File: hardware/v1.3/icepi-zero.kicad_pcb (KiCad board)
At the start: 4 copper layers, 65 x 30 mm, 159 parts, among them IC1 IS42S16160J-6BLI, J1 Conn_02x20_Counter_Clockwise, J2 GPDI_C_1.3, J3 USB_C_Receptacle_USB2.0_14P, J4 USB_C_Receptacle_USB2.0_14P, J5 USB_C_Receptacle_USB2.0_14P, J6 Micro_SD_Card_Det2, SW1 SW_Push, SW2 SW_Push, U1 ECP5-CABGA256, U10 TPD2EUSB30A, U12 W25Q128JVS, U2 TLV62569DBV, U3 TLV62569DBV, U4 TLV62569DBV, U5 TPD2EUSB30A, U6 PCA9306DC1, U7 TPD2EUSB30A, U8 TPD2EUSB30A, U9 FT231XQ, Y1 SG-8018CG 50.000000MHz

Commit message: 3.3V LDO
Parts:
- C34, L3: moved to B.Cu
- R11, R9: moved to F.Cu
- moved C34 53.2 mm to (160.7, 142.8)
- moved L3 49.3 mm to (160.7, 139.4), turned to -90 degrees
- moved R10 48.4 mm to (158.3, 140.3), turned to 90 degrees
- moved C35 47.4 mm to (159.3, 140.3), turned to 90 degrees
- moved U4 41.2 mm to (151.6, 136.6), turned to 90 degrees
- moved C33 39.9 mm to (149.0, 137.1), turned to 90 degrees
- moved R11 38.6 mm to (148.9, 135.1), turned to 180 degrees
- moved R9 6.53 mm to (151.2, 151.0), turned to 180 degrees
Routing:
- net Net-(U4-FB): track 0.00 -> 14.1 mm, vias 0 -> 1
- net +5V: track 59.4 -> 68.0 mm
- net +3V3: track 7.76 -> 12.9 mm
- net Net-(U3-FB): track 4.12 -> 6.06 mm
- net /SDRAM/D0: track 9.82 -> 8.54 mm

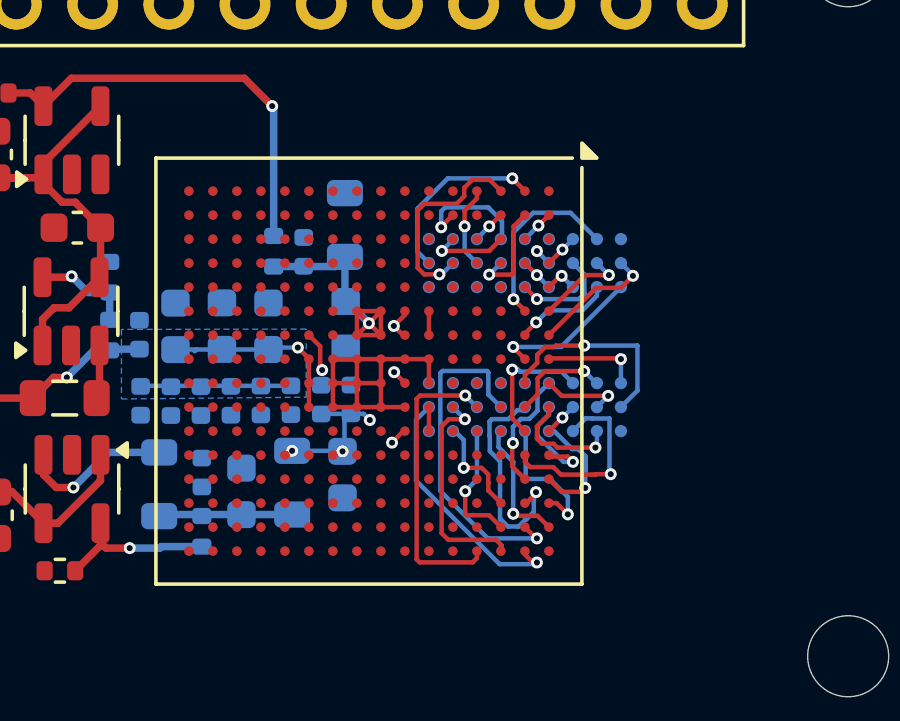
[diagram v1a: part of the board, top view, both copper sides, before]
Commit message: 3.3V memory fix
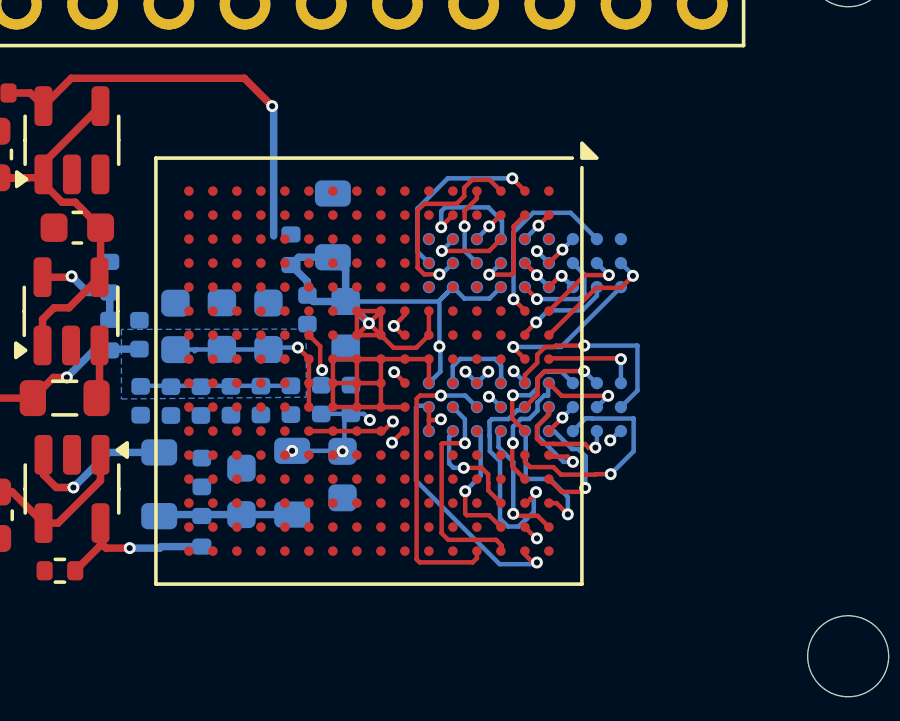
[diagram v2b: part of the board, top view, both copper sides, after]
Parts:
- moved C35 1.93 mm to (159.4, 142.3), turned to -90 degrees
- moved R10 0.58 mm to (158.8, 140.3)
- moved L3 0.40 mm to (160.2, 139.5)
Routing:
- net +3V3: track 12.9 -> 45.9 mm, vias 1 -> 8
- net /SDRAM/D6: track 11.3 -> 6.48 mm, vias 1 -> 2
- net GND: track 14.9 -> 17.9 mm
- net /SDRAM/~{CS}: track 6.53 -> 7.64 mm

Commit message: HDMI preparation
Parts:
- moved Y1 41.5 mm to (156.1, 136.4), turned to 180 degrees
- moved C1 40.5 mm to (156.9, 135.5), turned to 180 degrees
- moved C37 40.0 mm to (139.6, 150.9), turned to 90 degrees
- moved C38 38.9 mm to (140.0, 149.0), turned to 180 degrees
- moved C36 38.9 mm to (138.7, 150.9), turned to 90 degrees
- moved C39 38.2 mm to (140.0, 148.1), turned to 180 degrees
- moved C40 37.6 mm to (140.0, 147.2), turned to 180 degrees
- moved C41 37.0 mm to (140.0, 146.2), turned to 180 degrees
- moved C42 36.4 mm to (140.0, 145.3), turned to 180 degrees
- moved C43 35.9 mm to (140.0, 144.4), turned to 180 degrees
- moved R12 35.3 mm to (140.0, 143.5), turned to 0 degrees
- moved R13 34.8 mm to (140.0, 142.2), turned to 0 degrees
- moved R14 34.3 mm to (140.0, 141.3), turned to 0 degrees
- moved J2 32.5 mm to (136.7, 145.8), turned to -90 degrees
- moved C18 6.21 mm to (144.1, 152.9)
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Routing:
- net /SDRAM/A3: track 3.22 -> 14.6 mm
- net +5V: track 68.0 -> 77.1 mm
- net /GLOBAL_CLK: track 0.00 -> 3.78 mm
- net /GPDI/CONN_D2+: track 0.00 -> 3.53 mm
- net /GPDI/CONN_D2-: track 0.00 -> 3.02 mm
- net /SDRAM/D14: track 2.68 -> 5.45 mm
- net /GPDI/CONN_D1+: track 0.00 -> 2.35 mm
- net +3V3: track 45.9 -> 43.6 mm, vias 8 -> 9
- net Net-(J2-HPD): track 0.00 -> 2.07 mm
- net Net-(J2-UTILITY): track 0.00 -> 2.01 mm
- net Net-(J2-CEC): track 0.00 -> 2.00 mm
- net /GPDI/CONN_D1-: track 0.00 -> 1.99 mm
- net /GPDI/CONN_CK-: track 0.00 -> 1.98 mm
- net /GPDI/CONN_D0+: track 0.00 -> 1.94 mm
- net /GPDI/CONN_CK+: track 0.00 -> 1.77 mm
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
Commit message: HDMI preparation
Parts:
- R9: moved to B.Cu
- moved C36 14.6 mm to (124.5, 147.8)
- moved C38 14.6 mm to (125.8, 145.8)
- moved C40 14.6 mm to (125.8, 144.0)
- moved C41 14.6 mm to (125.8, 143.1)
- moved C42 14.6 mm to (125.8, 142.2)
- moved C43 14.6 mm to (125.8, 141.2)
- moved R12 14.6 mm to (125.8, 140.3)
- moved R13 14.6 mm to (125.8, 139.1)
- moved R14 14.6 mm to (125.8, 138.2)
- moved C39 14.6 mm to (125.8, 144.9)
- moved J2 14.6 mm to (122.5, 142.7)
- moved C37 14.6 mm to (125.4, 147.8)
- moved C18 1.27 mm to (143.2, 152.0), turned to 180 degrees
- moved R9 0.92 mm to (146.9, 153.0)
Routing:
- net /GPDI/GPDI_D0+: track 0.00 -> 38.8 mm
- net /GPDI/GPDI_CLK+: track 0.00 -> 37.3 mm
- net /GPDI/GPDI_D2+: track 0.00 -> 37.1 mm
- net /GPDI/GPDI_D1+: track 0.00 -> 36.8 mm
- net /GPDI/GPDI_D0-: track 0.00 -> 36.1 mm
- net /GPDI/GPDI_D1-: track 0.00 -> 36.0 mm
- net /GPDI/GPDI_CLK-: track 0.00 -> 35.6 mm
- net /GPDI/GPDI_D2-: track 0.00 -> 35.1 mm
- net +5V: track 77.1 -> 92.8 mm
- net Net-(U3-FB): track 6.06 -> 4.99 mm

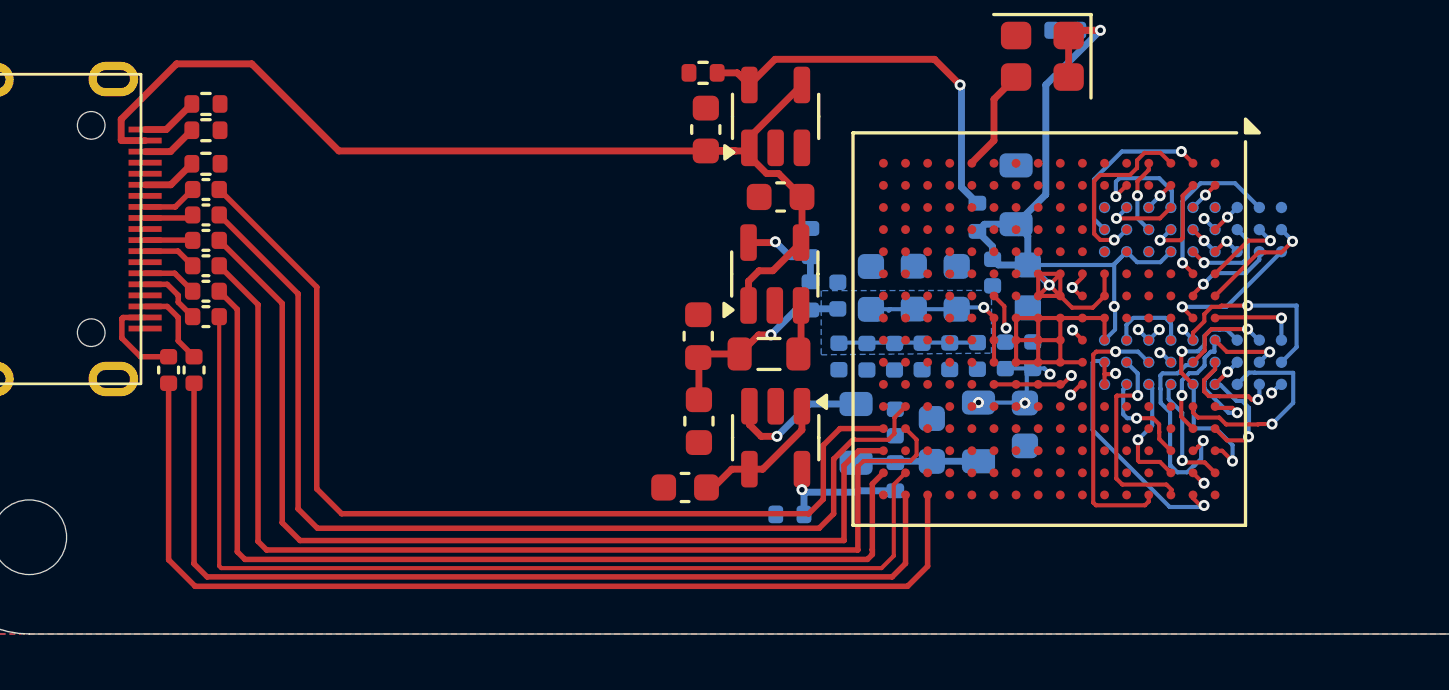
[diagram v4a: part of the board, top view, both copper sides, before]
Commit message: HDMI preparation, memory traces fix
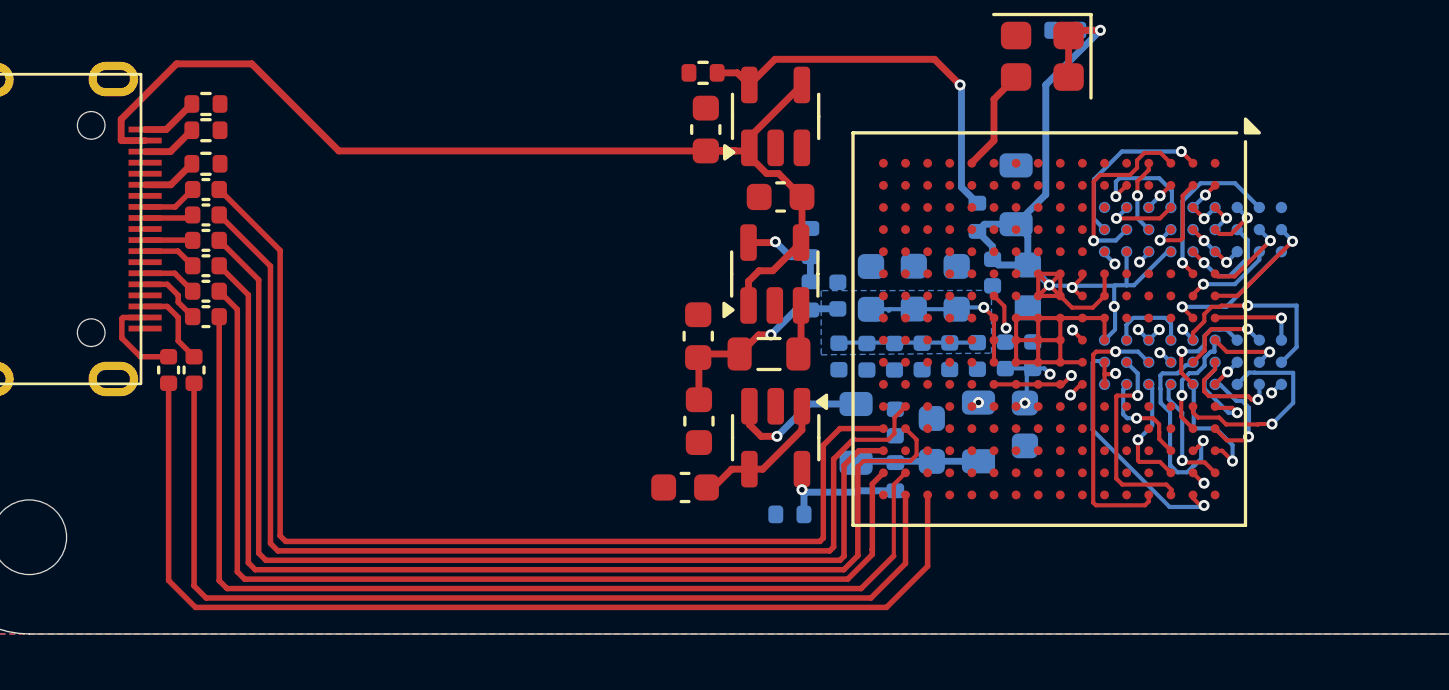
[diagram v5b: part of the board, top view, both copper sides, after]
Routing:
- net /SDRAM/A3: track 14.6 -> 3.22 mm
- net +3V3: track 43.6 -> 50.9 mm
- net /GPDI/GPDI_CLK-: track 35.6 -> 39.0 mm
- net /SDRAM/D14: track 5.45 -> 2.68 mm
- net /GPDI/GPDI_CLK+: track 37.3 -> 40.0 mm
- net /GPDI/GPDI_D0-: track 36.1 -> 38.2 mm
- net GND: track 17.9 -> 19.9 mm, vias 0 -> 2
- net /Power/FILTERED_2V5: track 13.5 -> 11.8 mm
- net /GPDI/GPDI_D0+: track 38.8 -> 40.2 mm
- net /SDRAM/DQM1: track 0.00 -> 1.14 mm, vias 0 -> 1
- net /GPDI/GPDI_D2-: track 35.1 -> 36.2 mm
- net /GPDI/GPDI_D2+: track 37.1 -> 38.2 mm
- net /GPDI/GPDI_D1-: track 36.0 -> 37.0 mm
- net /GPDI/GPDI_D1+: track 36.8 -> 37.7 mm
- net /SDRAM/A12: track 1.13 -> 2.01 mm
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
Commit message: GND fix
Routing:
- net GND: track 19.9 -> 24.8 mm
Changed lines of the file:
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@@
 	)
 	(segment
+		(start 159.925 151.495)
+		(end 160.151274 151.495)
+		(width 0.15)
+		(layer "F.Cu")
+		(net 16)
+	)
+	(segment
 		(start 157.525 147.495)
 		(end 155.125 147.495)
@@
 	)
 	(segment
+		(start 161.08 151.91)
+		(end 161.13 151.96)
+		(width 0.15)
+		(layer "F.Cu")
+		(net 16)
+	)
+	(segment
+		(start 160.301 140.719)
+		(end 161.901 140.719)
+		(width 0.15)
+		(layer "F.Cu")
+		(net 16)
+	)
+	(segment
+		(start 159.925 141.095)
+		(end 160.301 140.719)
+		(width 0.15)
+		(layer "F.Cu")
+		(net 16)
+	)
+	(segment
+		(start 161.901 140.719)
+		(end 162.325 140.295)
+		(width 0.15)
+		(layer "F.Cu")
+		(net 16)
+	)
+	(segment
 		(start 156.725 145.895)
 		(end 156.725 146.695)
@@
 	)
 	(segment
+		(start 160.151274 151.495)
+		(end 160.566274 151.91)
+		(width 0.15)
+		(layer "F.Cu")
+		(net 16)
+	)
+	(segment
+		(start 160.566274 151.91)
+		(end 161.08 151.91)
+		(width 0.15)
+		(layer "F.Cu")
+		(net 16)
+	)
+	(segment
 		(start 155.925 146.695)
 		(end 155.925 147.495)
@@
 	)
 	(segment
+		(start 161.13 151.96)
+		(end 161.13 152.73)
+		(width 0.15)
+		(layer "F.Cu")
+		(net 16)
+	)
+	(segment
 		(start 155.925 146.695)
 		(end 155.925 145.895)
@@
 	)
 	(segment
-		(start 160.761 141.293545)
-		(end 160.761 141.859)
+		(start 160.761 141.859)
+		(end 160.725 141.895)
 		(width 0.15)
 		(layer "B.Cu")
@@
 	)
 	(segment
-		(start 160.305 140.837545)
-		(end 160.761 141.293545)
+		(start 158.735 141.12291)
+		(end 158.81391 141.044)
 		(width 0.15)
 		(layer "B.Cu")
@@
 	)
 	(segment
-		(start 158.735 141.5)
-		(end 158.735 140.96509)
+		(start 160.761 141.293545)
+		(end 160.761 141.859)
 		(width 0.15)
 		(layer "B.Cu")
@@
 	)
 	(segment
-		(start 158.735 140.96509)
-		(end 158.862545 140.837545)
+		(start 158.81391 141.044)
+		(end 160.511455 141.044)
 		(width 0.15)
 		(layer "B.Cu")
@@
 	)
 	(segment
-		(start 160.761 141.859)
-		(end 160.725 141.895)
+		(start 158.735 141.5)
+		(end 158.735 141.12291)
 		(width 0.15)
 		(layer "B.Cu")
@@
 	)
 	(segment
-		(start 158.862545 140.837545)
-		(end 160.305 140.837545)
+		(start 160.511455 141.044)
+		(end 160.761 141.293545)
 		(width 0.15)
 		(layer "B.Cu")
@@
 	)
 	(segment
-		(start 159.769255 139.919)
-		(end 159.501 140.187255)
-		(width 0.15)
-		(layer "F.Cu")
-		(net 170)
-	)
-	(segment
-		(start 159.501 140.187255)
-		(end 159.501 140.464)
-		(width 0.15)
-		(layer "F.Cu")
-		(net 170)
-	)
-	(segment
 		(start 157.93 143.1)
 		(end 157.93 143.11)
@@
 	)
 	(segment
-		(start 158.169255 140.719)
-		(end 157.93 140.958255)
-		(width 0.15)
-		(layer "F.Cu")
-		(net 170)
-	)
-	(segment
-		(start 159.501 140.464)
-		(end 159.246 140.719)
+		(start 157.93 140.158255)
+		(end 158.169255 139.919)
 		(width 0.15)
 		(layer "F.Cu")
@@
 	)
 	(segment
-		(start 157.93 140.958255)
-		(end 157.93 143.1)
-		(width 0.15)
-		(layer "F.Cu")
-		(net 170)
-	)
-	(segment
-		(start 160.725 140.295)
+		(start 158.169255 139.919)
 		(end 160.349 139.919)
 		(width 0.15)
@@
 	(segment
 		(start 160.349 139.919)
-		(end 159.769255 139.919)
+		(end 160.725 140.295)
 		(width 0.15)
 		(layer "F.Cu")
@@
 	)
 	(segment
-		(start 159.246 140.719)
-		(end 158.169255 140.719)
+		(start 157.93 143.1)
+		(end 157.93 140.158255)
 		(width 0.15)
 		(layer "F.Cu")
@@
 	)
 	(segment
-		(start 158.749 148.726)
-		(end 158.749 151.698745)
-		(width 0.15)
-		(layer "F.Cu")
-		(net 211)
-	)
-	(segment
 		(start 158.775 148.7)
 		(end 158.749 148.726)
@@
 	)
 	(segment
-		(start 160.755 152.11)
-		(end 160.725 152.14)
+		(start 160.301 152.139255)
+		(end 160.301 152.295)
 		(width 0.15)
 		(layer "F.Cu")
@@
 	)
 	(segment
-		(start 158.969255 151.919)
-		(end 160.564 151.919)
+		(start 158.749 148.726)
+		(end 158.749 151.698745)
 		(width 0.15)
 		(layer "F.Cu")
@@
 	)
 	(segment
-		(start 160.725 152.14)
+		(start 160.301 152.295)
 		(end 160.725 152.295)
 		(width 0.15)
@@
 	)
 	(segment
-		(start 160.564 151.919)
-		(end 160.755 152.11)
+		(start 160.080745 151.919)
+		(end 160.301 152.139255)
+		(width 0.15)
+		(layer "F.Cu")
+		(net 211)
+	)
+	(segment
+		(start 158.969255 151.919)
+		(end 160.080745 151.919)
 		(width 0.15)
 		(layer "F.Cu")
